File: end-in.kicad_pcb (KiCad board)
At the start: 2 copper layers, 49.8 x 20 mm, 4 parts

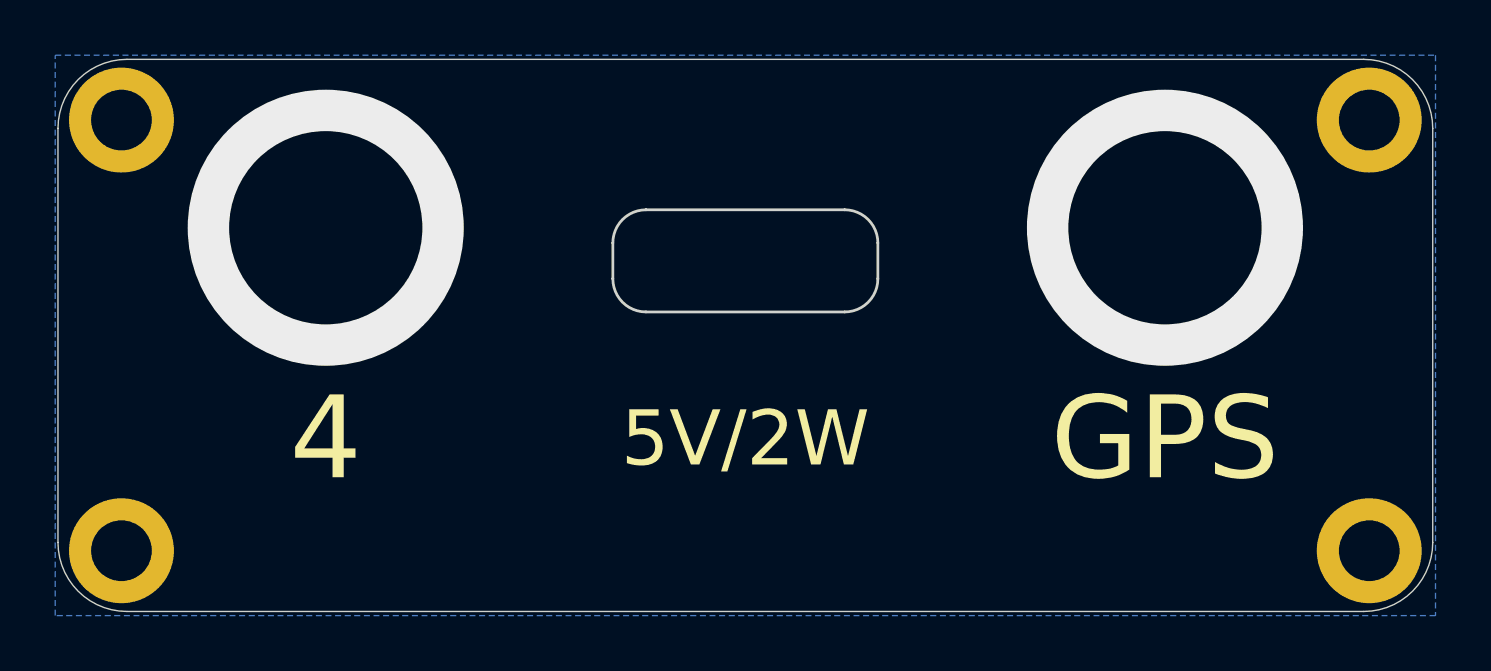
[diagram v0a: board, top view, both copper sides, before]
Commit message: Add bias resistors to comparators.
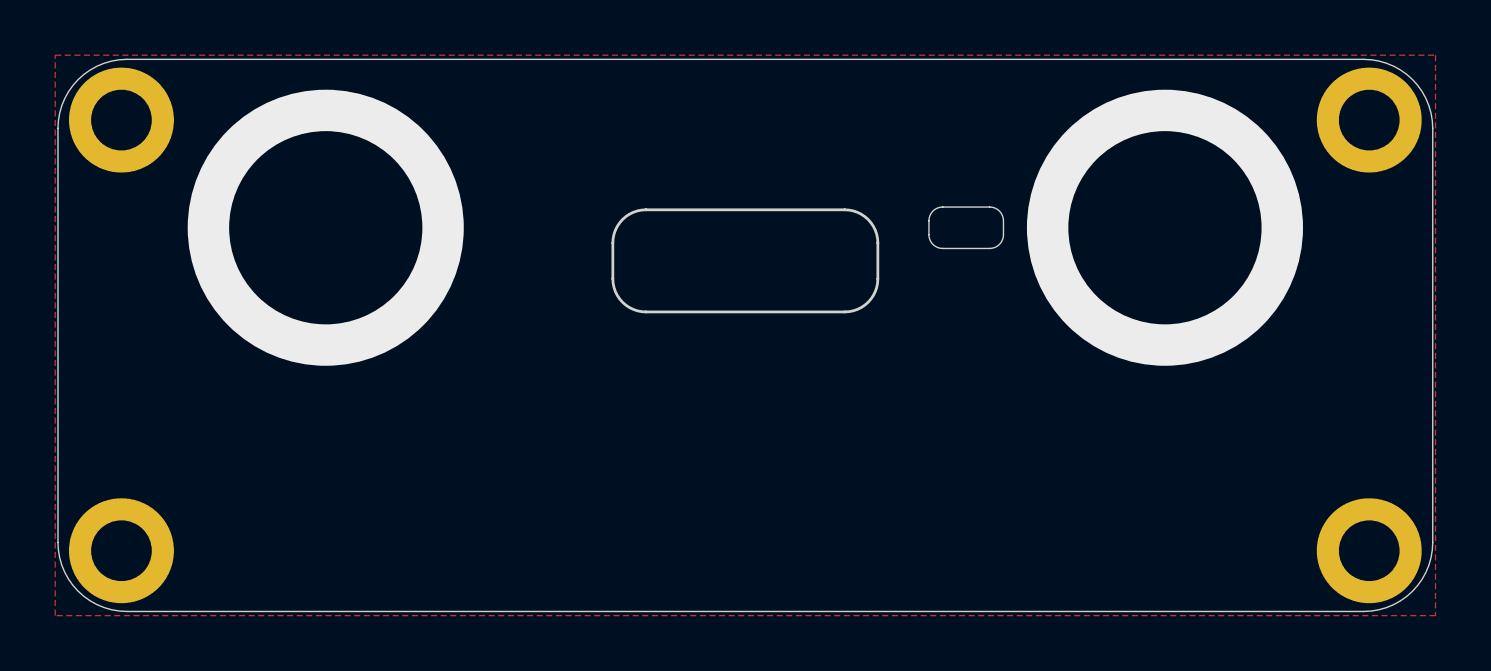
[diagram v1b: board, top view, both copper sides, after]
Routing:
- added copper zone on F.Cu, net GND
- removed copper zone on B.Cu, net GND
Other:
- outline, holes or cut-outs redrawn
- board text removed: "5V/2W"
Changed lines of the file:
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@@
 		(property ki_fp_filters "MountingHole*Pad*")
 		(sheetname "/")
-		(sheetfile "output.kicad_sch")
+		(sheetfile "end-in.kicad_sch")
 		(attr exclude_from_pos_files exclude_from_bom)
 		(fp_circle
@@
 		(property ki_fp_filters "MountingHole*Pad*")
 		(sheetname "/")
-		(sheetfile "output.kicad_sch")
+		(sheetfile "end-in.kicad_sch")
 		(attr exclude_from_pos_files exclude_from_bom)
 		(fp_circle
@@
 		(property ki_fp_filters "MountingHole*Pad*")
 		(sheetname "/")
-		(sheetfile "output.kicad_sch")
+		(sheetfile "end-in.kicad_sch")
 		(attr exclude_from_pos_files exclude_from_bom)
 		(fp_circle
@@
 		(property ki_fp_filters "MountingHole*Pad*")
 		(sheetname "/")
-		(sheetfile "output.kicad_sch")
+		(sheetfile "end-in.kicad_sch")
 		(attr exclude_from_pos_files exclude_from_bom)
 		(fp_circle
@@
 			(type default)
 		)
-		(layer "B.Mask")
+		(layer "F.Mask")
 	)
 	(gr_line
@@
 			(type default)
 		)
-		(layer "B.Mask")
+		(layer "F.Mask")
 	)
 	(gr_arc
@@
 			(type default)
 		)
-		(layer "B.Mask")
+		(layer "F.Mask")
 	)
 	(gr_line
@@
 			(type default)
 		)
-		(layer "B.Mask")
+		(layer "F.Mask")
 	)
 	(gr_arc
@@
 			(type default)
 		)
-		(layer "B.Mask")
+		(layer "F.Mask")
 	)
 	(gr_arc
@@
 			(type default)
 		)
-		(layer "B.Mask")
+		(layer "F.Mask")
 	)
 	(gr_line
@@
 			(type default)
 		)
-		(layer "B.Mask")
+		(layer "F.Mask")
 	)
 	(gr_line
@@
 			(type default)
 		)
-		(layer "B.Mask")
+		(layer "F.Mask")
 	)
 	(gr_arc
@@
 			(type default)
 		)
-		(layer "B.Mask")
+		(layer "F.Mask")
 	)
 	(gr_arc
@@
 	)
 	(gr_arc
+		(start 133.85 85.35)
+		(mid 134.203553 85.496447)
+		(end 134.35 85.85)
+		(stroke
+			(width 0.05)
+			(type default)
+		)
+		(layer "Edge.Cuts")
+	)
+	(gr_arc
+		(start 131.65 85.85)
+		(mid 131.796447 85.496447)
+		(end 132.15 85.35)
+		(stroke
+			(width 0.05)
+			(type default)
+		)
+		(layer "Edge.Cuts")
+	)
+	(gr_arc
 		(start 120.2 86.65)
 		(mid 120.551472 85.801472)
@@
 		(layer "Edge.Cuts")
 	)
+	(gr_line
+		(start 131.65 86.35)
+		(end 131.65 85.85)
+		(stroke
+			(width 0.05)
+			(type default)
+		)
+		(layer "Edge.Cuts")
+	)
+	(gr_line
+		(start 132.15 85.35)
+		(end 133.85 85.35)
+		(stroke
+			(width 0.05)
+			(type default)
+		)
+		(layer "Edge.Cuts")
+	)
 	(gr_arc
 		(start 100.1 82.5)
@@
 		(layer "Edge.Cuts")
 	)
+	(gr_line
+		(start 134.35 85.85)
+		(end 134.35 86.35)
+		(stroke
+			(width 0.05)
+			(type default)
+		)
+		(layer "Edge.Cuts")
+	)
 	(gr_arc
 		(start 129.8 87.95)
@@
 	)
 	(gr_arc
+		(start 134.35 86.35)
+		(mid 134.203553 86.703553)
+		(end 133.85 86.85)
+		(stroke
+			(width 0.05)
+			(type default)
+		)
+		(layer "Edge.Cuts")
+	)
+	(gr_arc
+		(start 132.15 86.85)
+		(mid 131.796447 86.703553)
+		(end 131.65 86.35)
+		(stroke
+			(width 0.05)
+			(type default)
+		)
+		(layer "Edge.Cuts")
+	)
+	(gr_line
+		(start 132.15 86.85)
+		(end 133.85 86.85)
+		(stroke
+			(width 0.05)
+			(type default)
+		)
+		(layer "Edge.Cuts")
+	)
+	(gr_arc
 		(start 102.6 100)
 		(mid 100.832233 99.267767)
@@
 		(layer "User.1")
 	)
+	(gr_rect
+		(start 132 85.6)
+		(end 134 86.6)
+		(stroke
+			(width 0.1)
+			(type default)
+		)
+		(fill no)
+		(layer "User.1")
+	)
 	(gr_line
 		(start 98.9 94.2)
@@
 		(start 98.6 85.7)
 		(end 101 85.7)
-		(stroke
-			(width 0.1)
-			(type default)
-		)
-		(layer "User.1")
-	)
-	(gr_line
-		(start 89.6 76.2)
-		(end 164.6 76.2)
 		(stroke
 			(width 0.1)
@@
 		(layer "User.1")
 	)
+	(gr_line
+		(start 133 85.5)
+		(end 133 87.1)
+		(stroke
+			(width 0.1)
+			(type default)
+		)
+		(layer "User.1")
+	)
 	(gr_circle
 		(center 109.8 86.1)
@@
 	)
 	(gr_text "GPS"
-		(at 140.2 93.75 0)
-		(layer "F.SilkS")
+		(at 109.8 93.75 -0)
+		(layer "B.SilkS")
 		(effects
 			(font
@@
 				(thickness 0.45)
 			)
+			(justify mirror)
 		)
 	)
 	(gr_text "4"
-		(at 109.8 93.75 0)
-		(layer "F.SilkS")
+		(at 140.2 93.75 -0)
+		(layer "B.SilkS")
 		(effects
 			(font
@@
 				(thickness 0.45)
 			)
-		)
-	)
-	(gr_text "5V/2W"
-		(at 125 93.75 0)
-		(layer "F.SilkS")
-		(effects
-			(font
-				(size 2 2)
-				(thickness 0.3)
-			)
+			(justify mirror)
 		)
 	)
@@
 		(layer "User.1")
 		(pts
+			(xy 125 100.475) (xy 133 100.475)
+		)
+		(height -26.675)
+		(orientation 0)
+		(format
+			(prefix "")
+			(suffix "")
+			(units 3)
+			(units_format 0)
+			(precision 4)
+			(suppress_zeroes yes)
+		)
+		(style
+			(thickness 0.1)
+			(arrow_length 1.27)
+			(text_position_mode 0)
+			(arrow_direction outward)
+			(extension_height 0.58642)
+			(extension_offset 0.5)
+			(keep_text_aligned yes)
+		)
+		(gr_text "8"
+			(at 129 72.65 0)
+			(layer "User.1")
+			(effects
+				(font
+					(size 1 1)
+					(thickness 0.15)
+				)
+			)
+		)
+	)
+	(dimension
+		(type orthogonal)
+		(layer "User.1")
+		(pts
 			(xy 153.2 85.7) (xy 153 86.1)
 		)
@@
 		(net 1)
 		(net_name "GND")
-		(layer "B.Cu")
+		(layer "F.Cu")
 		(name "Back")
 		(hatch edge 0.5)

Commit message: Use a plated hole for the LED panel opening
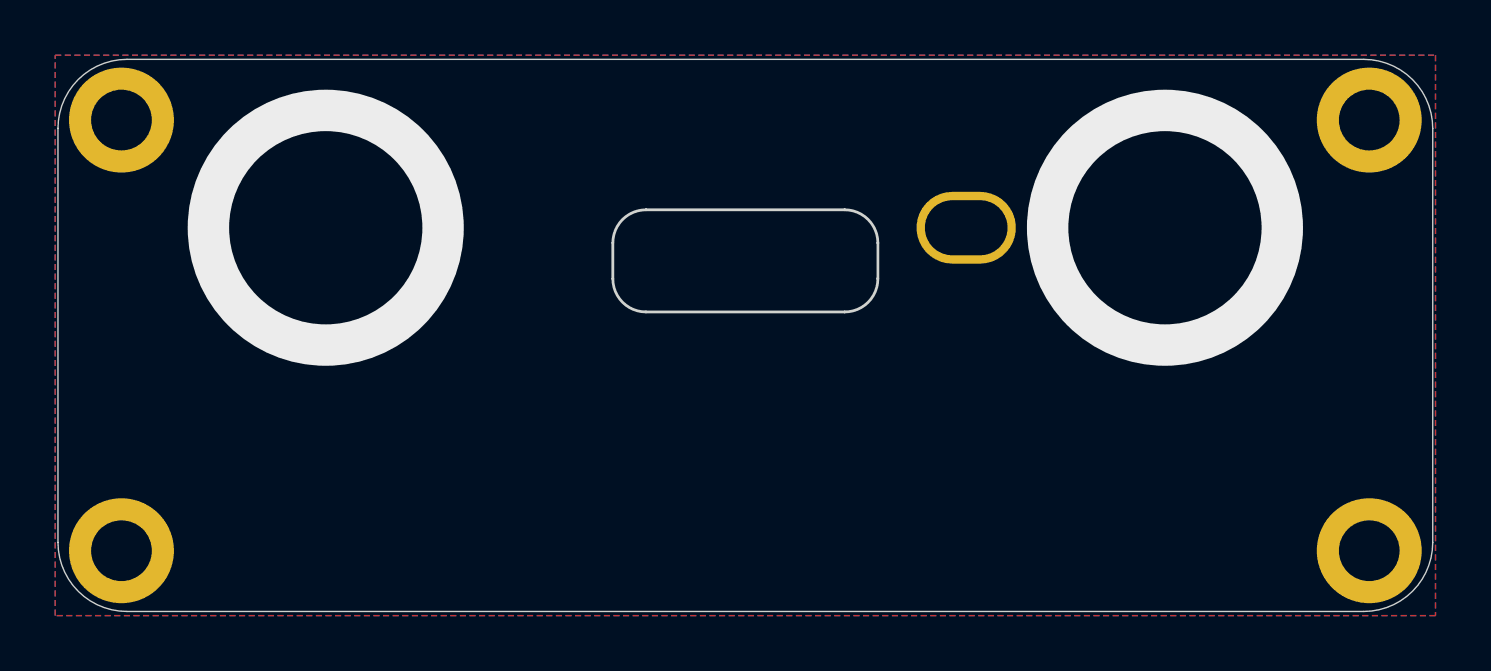
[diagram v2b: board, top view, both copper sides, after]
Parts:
- added H5: LED Hole, Parts:LED_Hole, F.Cu at (133.0, 86.1)
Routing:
- added copper zone on B.Cu, net GND
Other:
- outline, holes or cut-outs redrawn
- board text added: "freak"
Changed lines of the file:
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@@
+		(embedded_fonts no)
+	)
+	(footprint "Parts:LED_Hole"
+		(layer "F.Cu")
+		(at 133 86.1)
+		(descr "Panel hole for edge mount LED.")
+		(property "Reference" "H5"
+			(at 0 -0.5 0)
+			(unlocked yes)
+			(layer "F.SilkS")
+			(hide yes)
+			(effects
+				(font
+					(size 1 1)
+					(thickness 0.1)
+				)
+			)
+		)
+		(property "Value" "LED Hole"
+			(at 0 1 0)
+			(unlocked yes)
+			(layer "F.Fab")
+			(effects
+				(font
+					(size 1 1)
+					(thickness 0.15)
+				)
+			)
+		)
+		(property "Datasheet" "~"
+			(at 0 0 0)
+			(unlocked yes)
+			(layer "F.Fab")
+			(hide yes)
+			(effects
+				(font
+					(size 1 1)
+					(thickness 0.15)
+				)
+			)
+		)
+		(property "Description" "Mounting Hole with connection"
+			(at 0 0 0)
+			(unlocked yes)
+			(layer "F.Fab")
+			(hide yes)
+			(effects
+				(font
+					(size 1 1)
+					(thickness 0.15)
+				)
+			)
+		)
+		(property "JLCPCB" ""
+			(at 0 0 0)
+			(unlocked yes)
+			(layer "F.Fab")
+			(hide yes)
+			(effects
+				(font
+					(size 1 1)
+					(thickness 0.15)
+				)
+			)
+		)
+		(property ki_fp_filters "MountingHole*Pad*")
+		(sheetname "/")
+		(sheetfile "end-in.kicad_sch")
+		(attr smd exclude_from_bom)
+		(fp_text user "${REFERENCE}"
+			(at 0 2.5 0)
+			(unlocked yes)
+			(layer "F.Fab")
+			(effects
+				(font
+					(size 1 1)
+					(thickness 0.15)
+				)
+			)
+		)
+		(pad "1" thru_hole roundrect
+			(at 0 0)
+			(size 3.6 2.6)
+			(drill oval 3 2)
+			(layers "*.Cu" "*.Mask")
+			(remove_unused_layers no)
+			(roundrect_rratio 0.5)
+			(net 1 "GND")
+			(pinfunction "1")
+			(pintype "input")
+		)
 		(embedded_fonts no)
 	)
@@
 	)
 	(gr_arc
-		(start 133.85 85.35)
-		(mid 134.203553 85.496447)
-		(end 134.35 85.85)
-		(stroke
-			(width 0.05)
-			(type default)
-		)
-		(layer "Edge.Cuts")
-	)
-	(gr_arc
-		(start 131.65 85.85)
-		(mid 131.796447 85.496447)
-		(end 132.15 85.35)
-		(stroke
-			(width 0.05)
-			(type default)
-		)
-		(layer "Edge.Cuts")
-	)
-	(gr_arc
 		(start 120.2 86.65)
 		(mid 120.551472 85.801472)
@@
 		(layer "Edge.Cuts")
 	)
-	(gr_line
-		(start 131.65 86.35)
-		(end 131.65 85.85)
-		(stroke
-			(width 0.05)
-			(type default)
-		)
-		(layer "Edge.Cuts")
-	)
-	(gr_line
-		(start 132.15 85.35)
-		(end 133.85 85.35)
-		(stroke
-			(width 0.05)
-			(type default)
-		)
-		(layer "Edge.Cuts")
-	)
 	(gr_arc
 		(start 100.1 82.5)
@@
 		(layer "Edge.Cuts")
 	)
-	(gr_line
-		(start 134.35 85.85)
-		(end 134.35 86.35)
-		(stroke
-			(width 0.05)
-			(type default)
-		)
-		(layer "Edge.Cuts")
-	)
 	(gr_arc
 		(start 129.8 87.95)
@@
 	)
 	(gr_arc
-		(start 134.35 86.35)
-		(mid 134.203553 86.703553)
-		(end 133.85 86.85)
-		(stroke
-			(width 0.05)
-			(type default)
-		)
-		(layer "Edge.Cuts")
-	)
-	(gr_arc
-		(start 132.15 86.85)
-		(mid 131.796447 86.703553)
-		(end 131.65 86.35)
-		(stroke
-			(width 0.05)
-			(type default)
-		)
-		(layer "Edge.Cuts")
-	)
-	(gr_line
-		(start 132.15 86.85)
-		(end 133.85 86.85)
-		(stroke
-			(width 0.05)
-			(type default)
-		)
-		(layer "Edge.Cuts")
-	)
-	(gr_arc
 		(start 102.6 100)
 		(mid 100.832233 99.267767)
@@
 			(type default)
 		)
-		(layer "User.1")
-	)
-	(gr_rect
-		(start 132 85.6)
-		(end 134 86.6)
-		(stroke
-			(width 0.1)
-			(type default)
-		)
-		(fill no)
 		(layer "User.1")
 	)
@@
 		)
 	)
+	(gr_text "freak"
+		(at 109.675 97 0)
+		(layer "B.SilkS")
+		(effects
+			(font
+				(size 2 2)
+				(thickness 0.3)
+				(bold yes)
+				(italic yes)
+			)
+			(justify mirror)
+		)
+	)
 	(dimension
 		(type orthogonal)
@@
 		(net 1)
 		(net_name "GND")
-		(layer "F.Cu")
+		(layers "F.Cu" "B.Cu")
 		(name "Back")
 		(hatch edge 0.5)
-		(connect_pads
+		(connect_pads yes
 			(clearance 0.2)
 		)
